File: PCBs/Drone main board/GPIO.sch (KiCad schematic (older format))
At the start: 7 parts, among them J1001 Conn_02x10, J1002 Conn_02x07, J1003 Conn_02x10, J1004 Conn_02x05

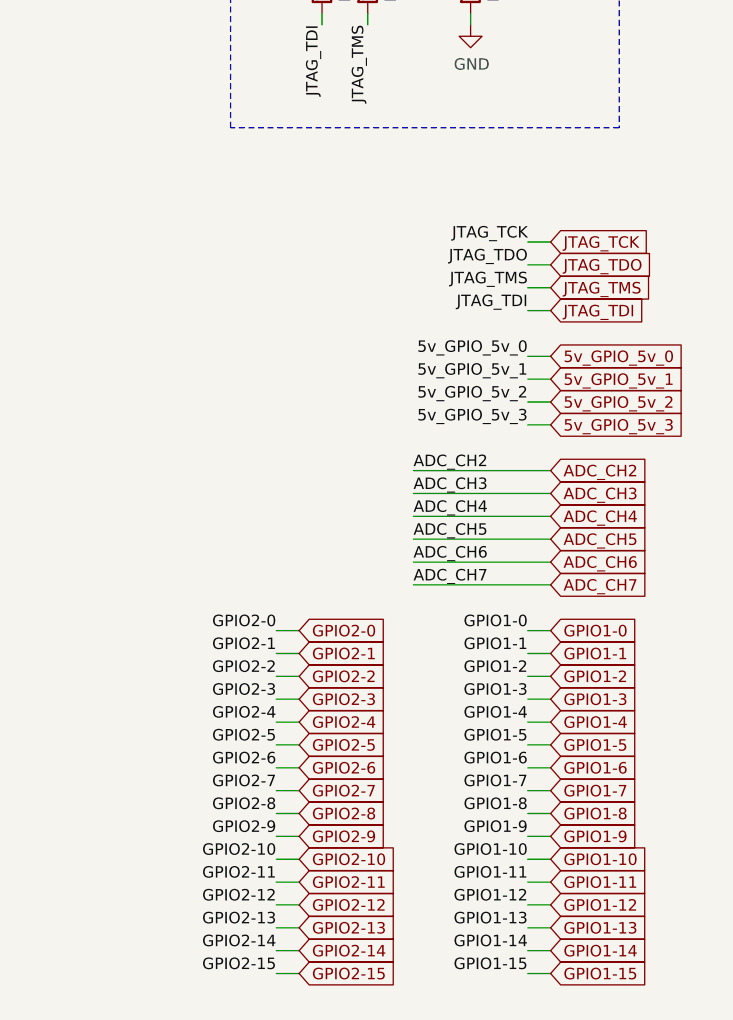
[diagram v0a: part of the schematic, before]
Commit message: Some cleanup, and PCB antenna removal.
Last edits before asking for reddit feedback.

Signed-off-by: Eldalote.Electronics <Eldalote.Electronics@gmail.com>
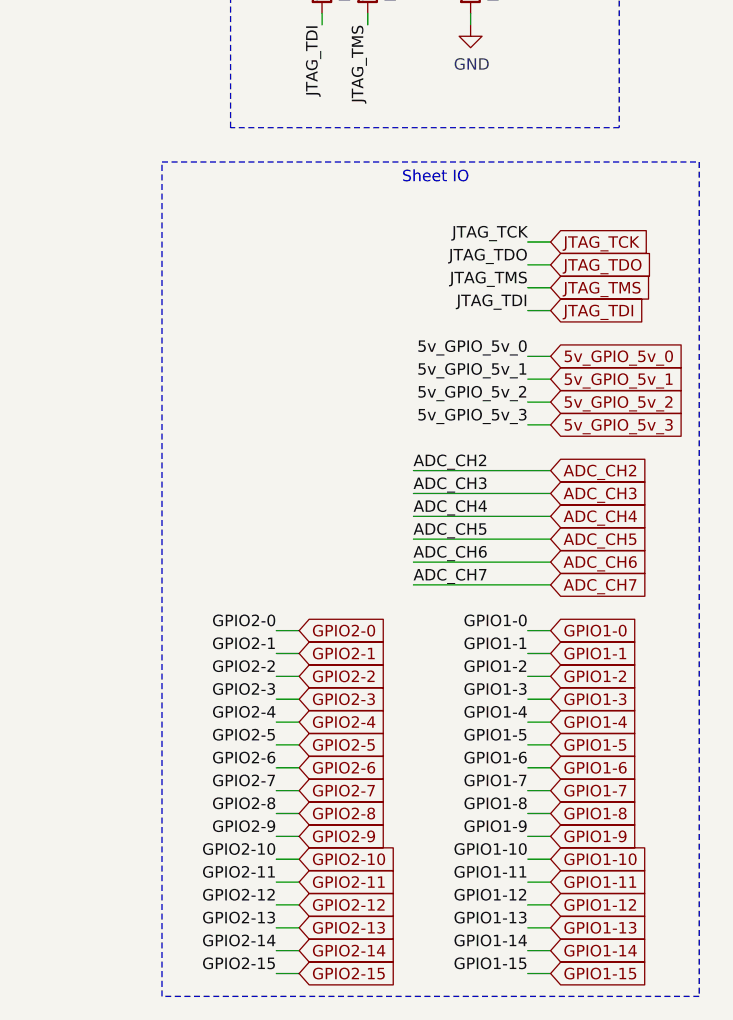
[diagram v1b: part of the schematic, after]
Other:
- note added: "Sheet IO"
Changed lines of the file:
@@
 Text GLabel 9000 6300 2    50   Input ~ 0
 GPIO2-15
+Wire Notes Line
+	8400 2750 10750 2750
+Wire Notes Line
+	10750 2750 10750 6400
+Wire Notes Line
+	10750 6400 8400 6400
+Wire Notes Line
+	8400 6400 8400 2750
+Text Notes 9450 2850 0    50   ~ 0
+Sheet IO
 $EndSCHEMATC

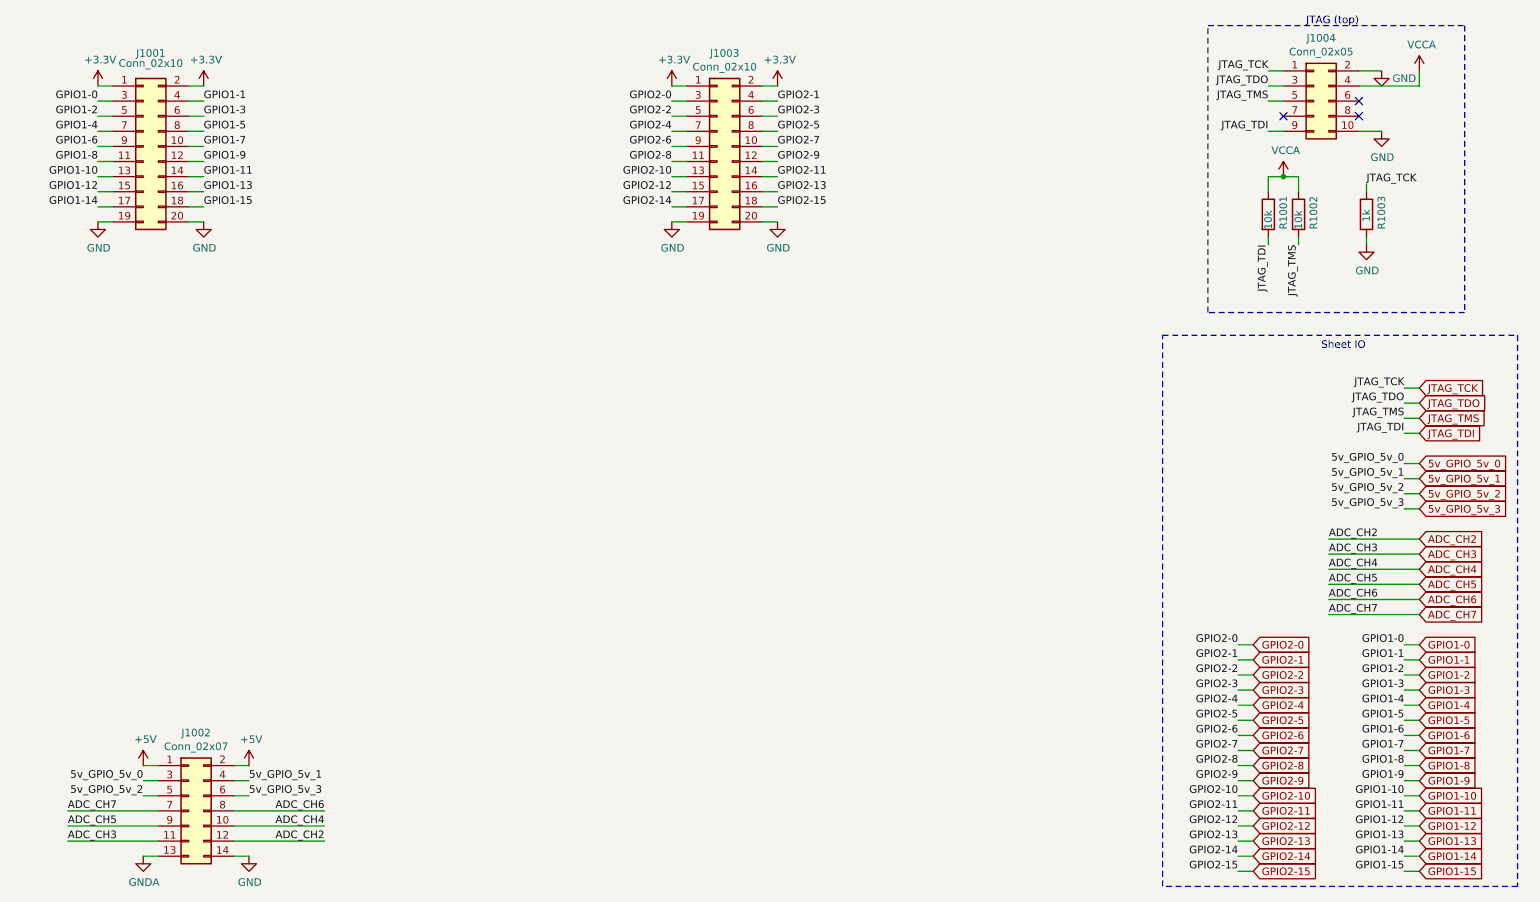
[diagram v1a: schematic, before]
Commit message: Finished (?) the schematic check and update. Next: PCB update
Signed-off-by: Eldalote.Electronics <Eldalote.Electronics@gmail.com>
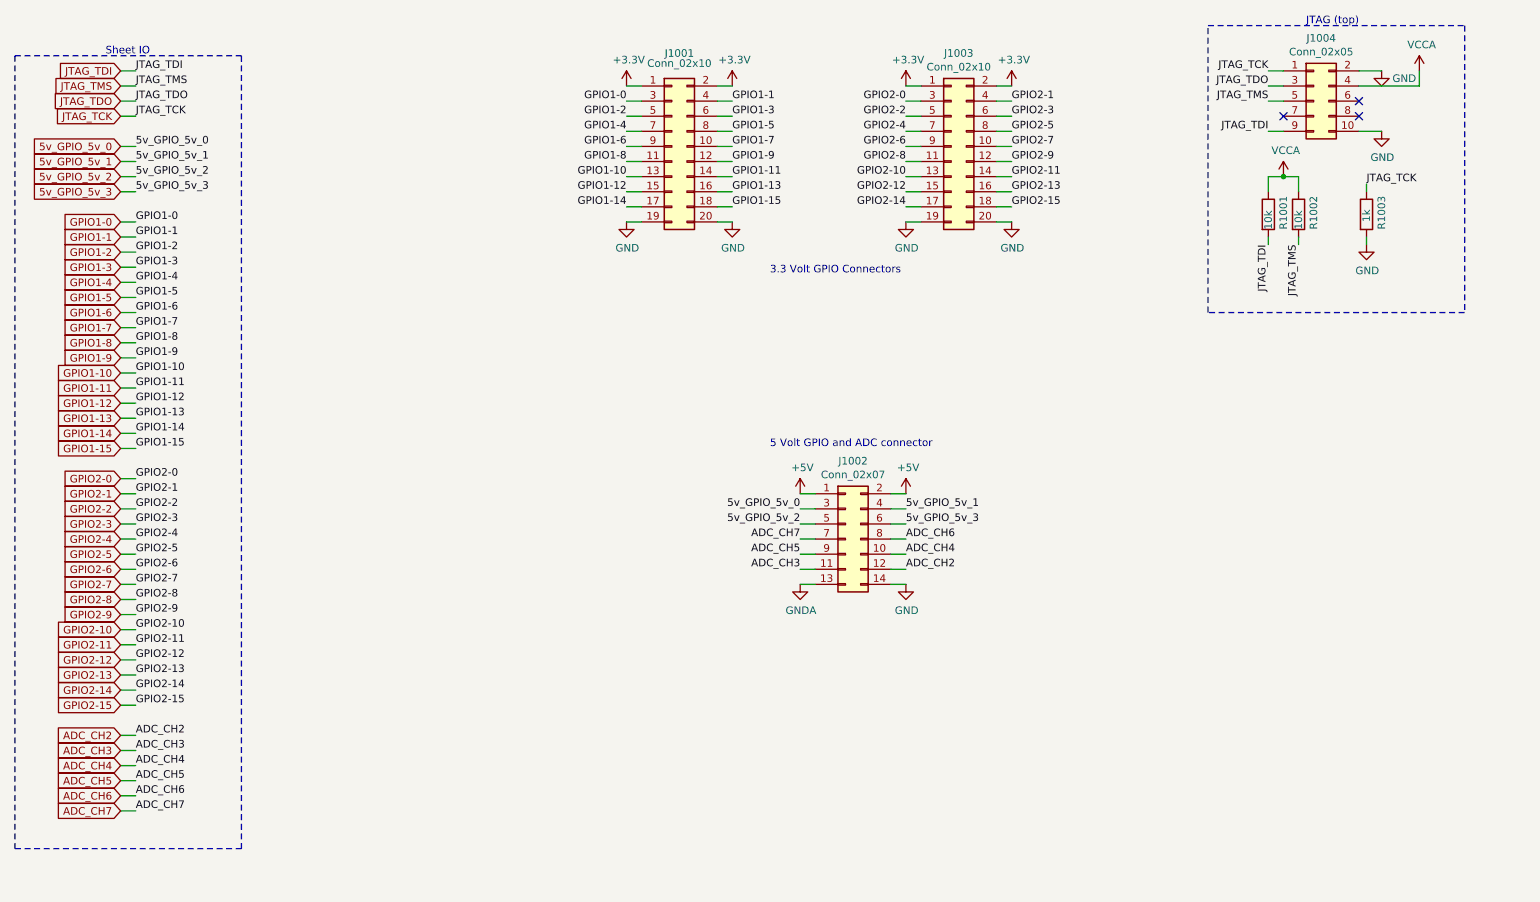
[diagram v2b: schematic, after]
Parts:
- R1001, R1002: LCSC C25744 -> (none); MfNr (none) -> RC0402FR-0710KL
- R1003: LCSC C11702 -> (none); MfNr (none) -> RC0402FR-071KL
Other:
- note added: "3.3 Volt GPIO Connectors"
- note added: "5 Volt GPIO and ADC connector"
- moved on the sheet: J1001, J1002, J1003
